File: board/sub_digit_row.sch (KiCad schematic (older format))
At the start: 86 parts, among them Q601 Q_PMOS_GSD, Q602 Q_PMOS_GSD, Q603 Q_PMOS_GSD, Q604 Q_PMOS_GSD, Q605 Q_PMOS_GSD, Q606 Q_PMOS_GSD, Q607 Q_PMOS_GSD, Q608 Q_PMOS_GSD, U601 TPIC6D595, U602 TPIC6D595, U603 TPIC6D595

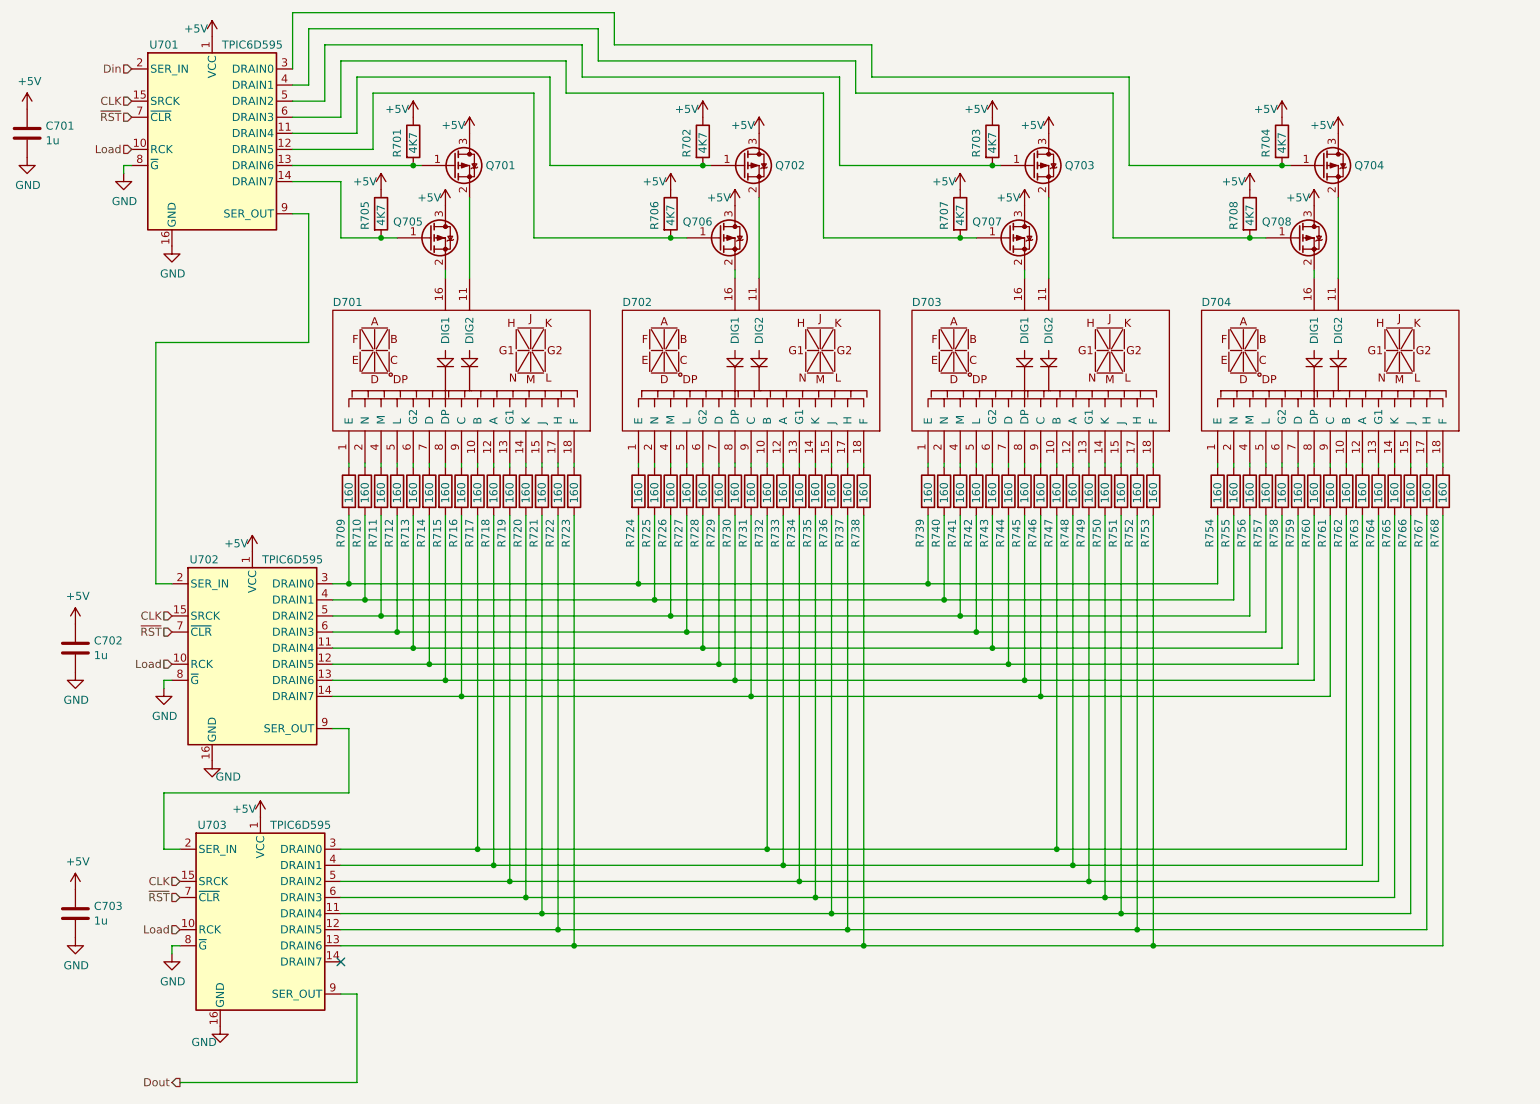
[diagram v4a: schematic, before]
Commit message: Started picking footprints. Merged many components.
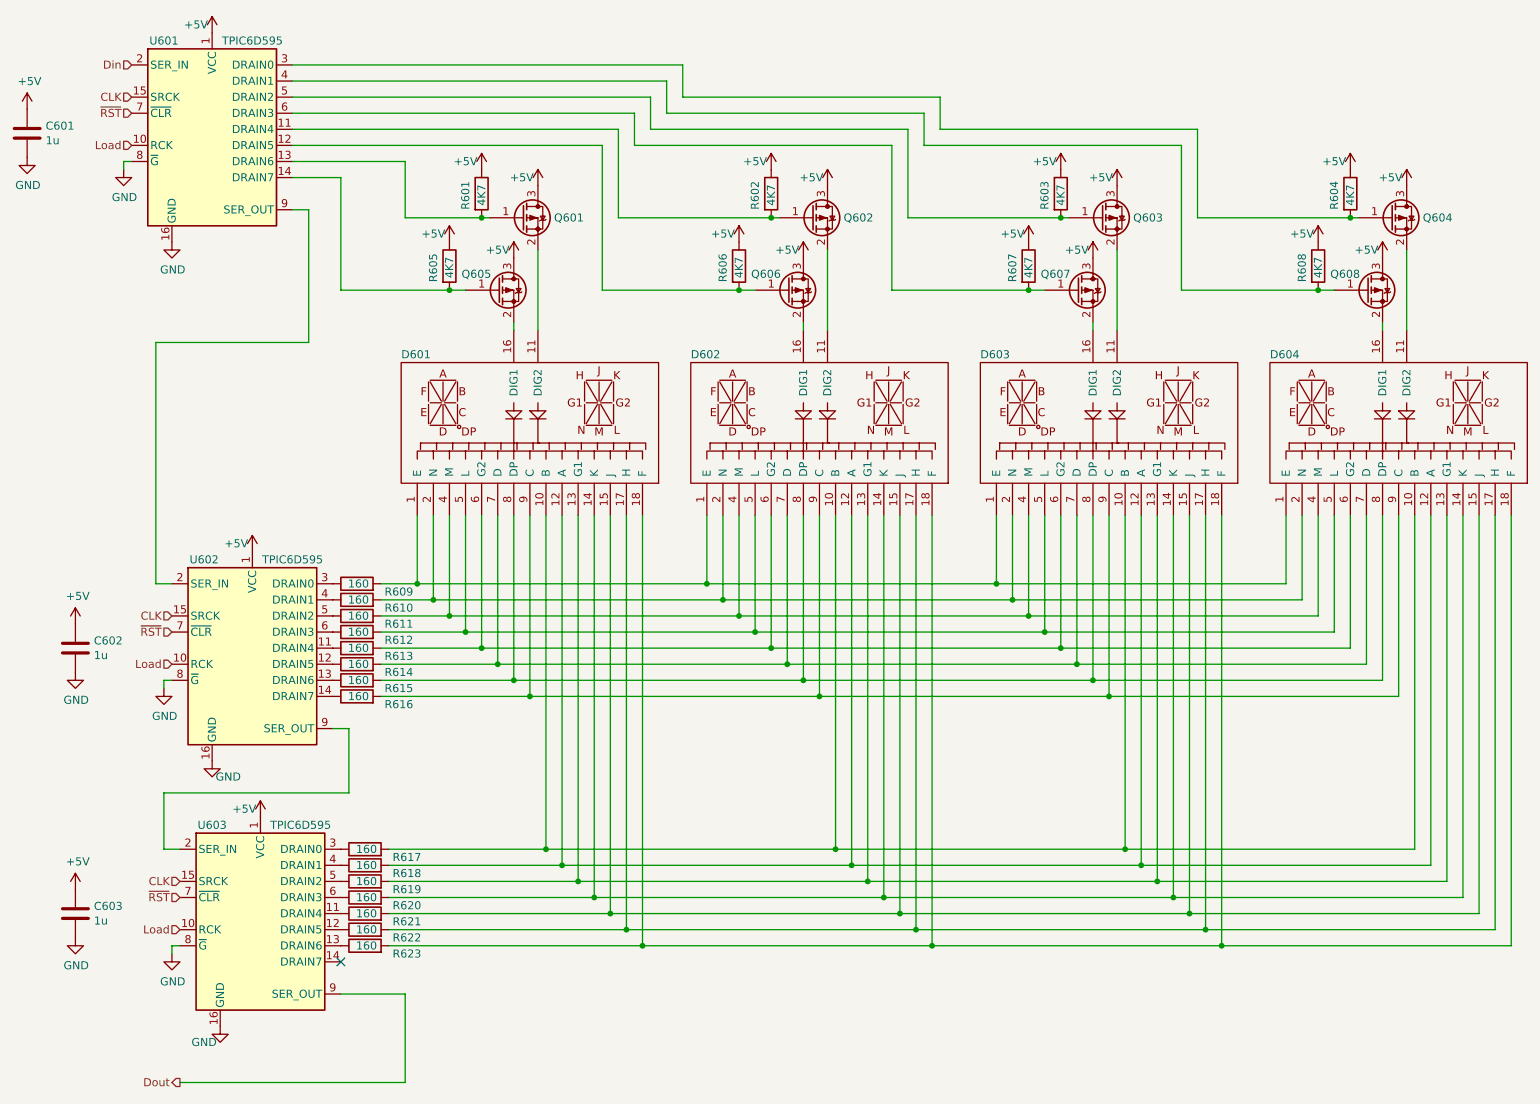
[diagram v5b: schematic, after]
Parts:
- removed R624, R625, R626, R627, R628, R629, R630, R631, R632, R633, R634, R635, R636, R637, R638, R639, R640, R641, R642, R643, R644, R645, R646, R647, R648, R649, R650, R651, R652, R653, R654, R655, R656, R657, R658, R659, R660, R661, R662, R663, R664, R665, R666, R667, R668: 160, symbol Device:R
- U601, U602, U603: footprint (none) -> Package_SO:SOIC-16_3.9x9.9mm_P1.27mm
- renumbered R623 to R609, R622 to R610, R621 to R611, R620 to R612, R619 to R613, R618 to R614, R617 to R615, R615 to R617, R614 to R618, R613 to R619, R612 to R620, R611 to R621, R610 to R622, R609 to R623
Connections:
- net at D602.1 (E): now also D601.1 (E), D603.1 (E), D604.1 (E), R609.2
- net at D602.10 (B): now also D601.10 (B), D603.10 (B), D604.10 (B), R617.2
- net at D602.12 (A): now also D601.12 (A), D603.12 (A), D604.12 (A), R618.2
- net at D602.13 (G1): now also D601.13 (G1), D603.13 (G1), D604.13 (G1), R619.2
- net at D602.14 (K): now also D601.14 (K), D603.14 (K), D604.14 (K), R620.2
- net at D602.15 (J): now also D601.15 (J), D603.15 (J), D604.15 (J), R621.2
- net at D602.17 (H): now also D601.17 (H), D603.17 (H), D604.17 (H), R622.2
- net at D602.18 (F): now also D601.18 (F), D603.18 (F), D604.18 (F), R623.2
- net at D602.2 (N): now also D601.2 (N), D603.2 (N), D604.2 (N), R610.2
- net at D602.4 (M): now also D601.4 (M), D603.4 (M), D604.4 (M), R611.2
- net at D602.5 (L): now also D601.5 (L), D603.5 (L), D604.5 (L), R612.2
- net at D602.6 (G2): now also D601.6 (G2), D603.6 (G2), D604.6 (G2), R613.2
- net at D602.7 (D): now also D601.7 (D), D603.7 (D), D604.7 (D), R614.2
- net at D602.8 (DP): now also D601.8 (DP), D603.8 (DP), D604.8 (DP), R615.2
- net at D602.9 (C): now also D601.9 (C), D603.9 (C), D604.9 (C), R616.2
- net at U603.11 (DRAIN4): now also R621.1; no longer R611.2
- net at U603.12 (DRAIN5): now also R622.1; no longer R610.2
- net at U603.13 (DRAIN6): now also R623.1; no longer R609.2
- net at U603.3 (DRAIN0): now also R617.1; no longer R615.2
- net at U603.4 (DRAIN1): now also R618.1; no longer R614.2
- net at U603.5 (DRAIN2): now also R619.1; no longer R613.2
- net at U603.6 (DRAIN3): now also R620.1; no longer R612.2
- net at R615.1: now also U602.13 (DRAIN6); no longer D601.10 (B)
- net at R614.1: now also U602.12 (DRAIN5); no longer D601.12 (A)
- net at R613.1: now also U602.11 (DRAIN4); no longer D601.13 (G1)
- net at R612.1: now also U602.6 (DRAIN3); no longer D601.14 (K)
- net at R611.1: now also U602.5 (DRAIN2); no longer D601.15 (J)
- net at R610.1: now also U602.4 (DRAIN1); no longer D601.17 (H)
- net at R609.1: now also U602.3 (DRAIN0); no longer D601.18 (F)
- net at R616.1: now also U602.14 (DRAIN7); no longer D601.9 (C)
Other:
- moved on the sheet: D601, D602, D603, D604, Q601, Q602, Q603, Q604, Q605, Q606, Q607, Q608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

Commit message: More footprints done. Went with simpler test-pads.
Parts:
- Q601, Q602, Q603, Q604, Q605, Q606, Q607, Q608: footprint (none) -> Package_TO_SOT_SMD:SOT-23
- R609, R610, R611, R612, R613, R614, R615, R616, R617, R618, R619, R620, R621, R622, R623: footprint (none) -> Resistor_SMD:R_1206_3216Metric

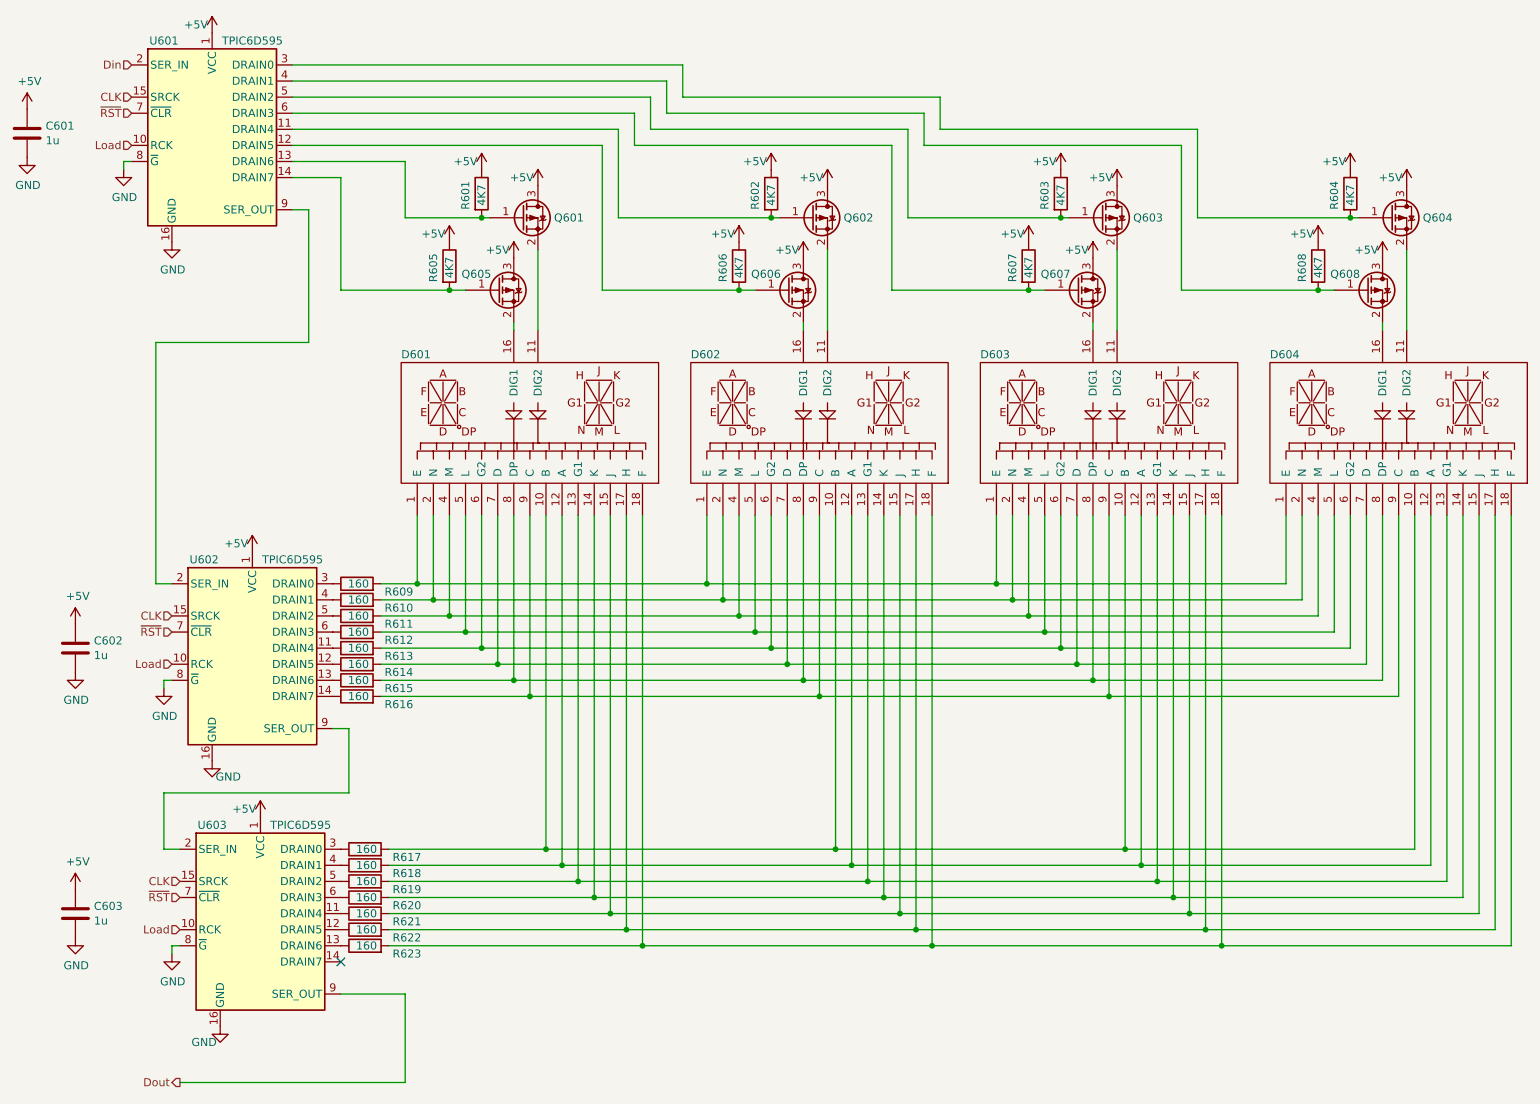
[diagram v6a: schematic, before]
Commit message: Fixed swapped pin and some labels
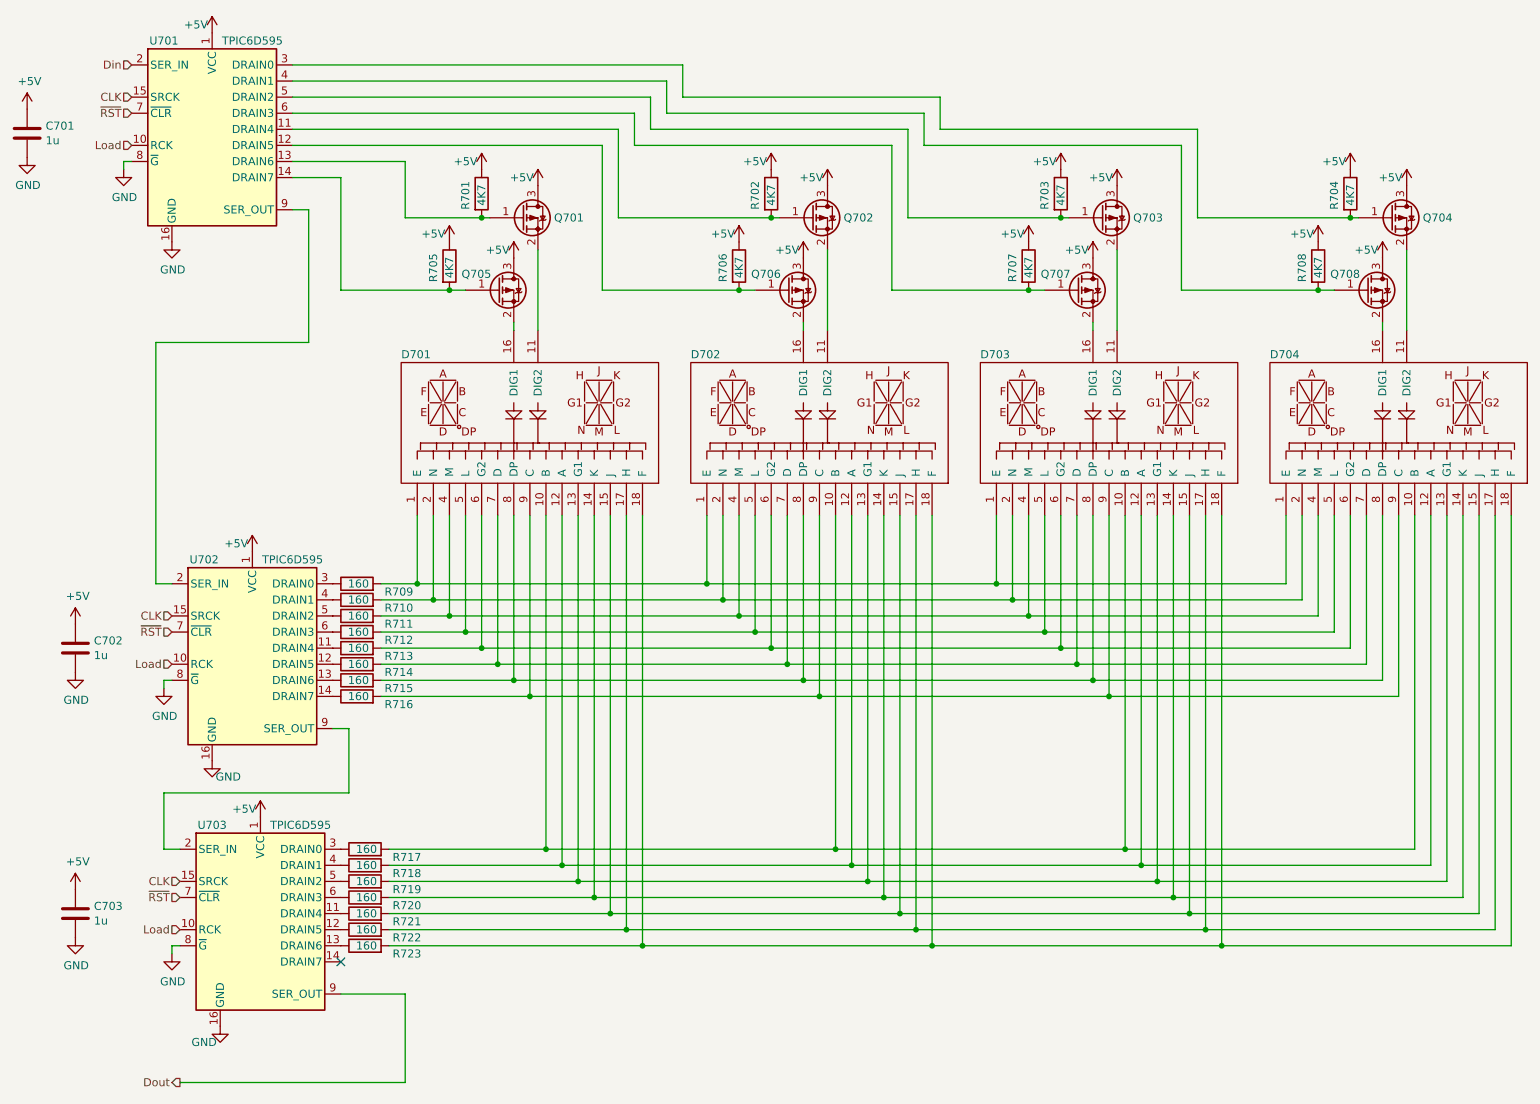
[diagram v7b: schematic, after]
